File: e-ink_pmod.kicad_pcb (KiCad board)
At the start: 2 copper layers, 45.7 x 20.3 mm, 1 part

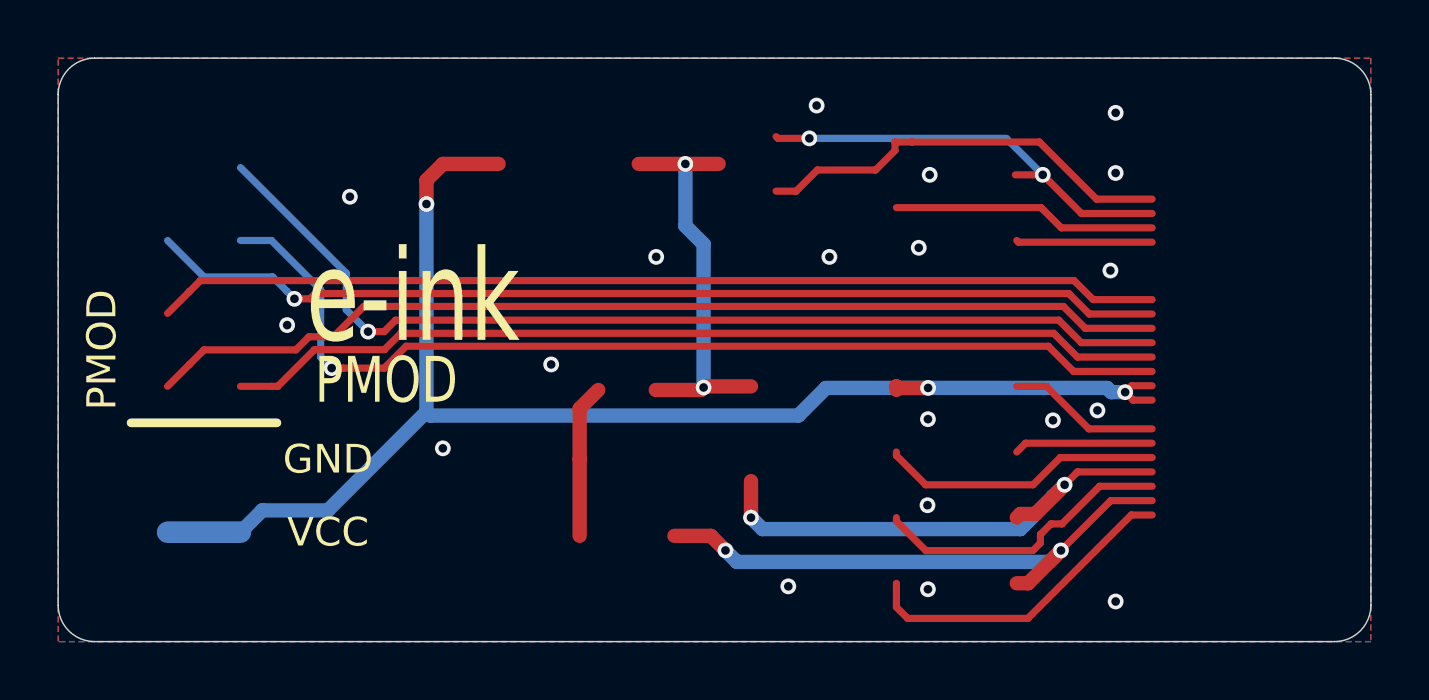
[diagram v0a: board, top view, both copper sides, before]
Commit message: Added SPI SRAM for framebuffer
Also updated to new KiCad version 6 file formats
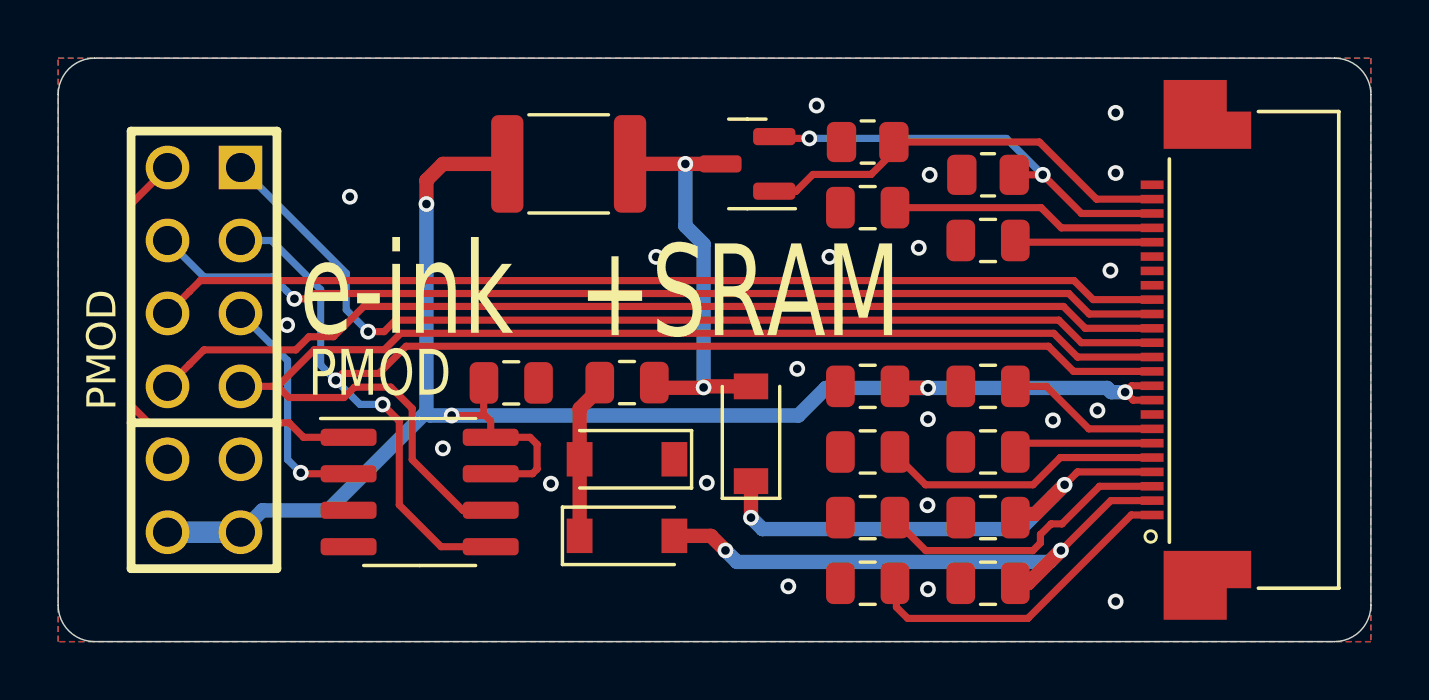
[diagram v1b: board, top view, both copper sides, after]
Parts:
- added C1: 1uF, Capacitor_SMD:C_0805_2012Metric, F.Cu at (114.6, 75.1)
- added C10: 2.2uF, Capacitor_SMD:C_0805_2012Metric, F.Cu at (114.6, 81.3)
- added C11: 1uF, Capacitor_SMD:C_0805_2012Metric, F.Cu at (118.7, 83.6)
- added C12: 1uF, Capacitor_SMD:C_0805_2012Metric, F.Cu at (102.1, 81.2)
- added C2: 1uF, Capacitor_SMD:C_0805_2012Metric, F.Cu at (118.7, 76.2)
- added C3: 1uF, Capacitor_SMD:C_0805_2012Metric, F.Cu at (118.7, 81.3)
- added C4: 1uF, Capacitor_SMD:C_0805_2012Metric, F.Cu at (114.6, 83.6)
- added C5: 1uF, Capacitor_SMD:C_0805_2012Metric, F.Cu at (114.6, 85.9)
- added C6: 1uF, Capacitor_SMD:C_0805_2012Metric, F.Cu at (114.6, 88.1)
- added C7: 1uF, Capacitor_SMD:C_0805_2012Metric, F.Cu at (118.7, 85.9)
- added C8: 1uF, Capacitor_SMD:C_0805_2012Metric, F.Cu at (118.7, 88.1)
- added C9: 1uF, Capacitor_SMD:C_0805_2012Metric, F.Cu at (106.2, 81.2)
- added D1: D_Schottky, Diode_SMD:D_SOD-123, F.Cu at (106.2, 86.5)
- added D2: D_Schottky, Diode_SMD:D_SOD-123, F.Cu at (106.2, 83.8)
- added D3: D_Schottky, Diode_SMD:D_SOD-123, F.Cu at (110.5, 82.9)
- added G***: LOGO, Aesthetics:HXR_logo_small, B.Cu at (126.8, 80.0)
- added L1: 68uH, Inductor_SMD:L_1812_4532Metric, F.Cu at (104.1, 73.5)
- added Q1: Q_NMOS_GSD, Package_TO_SOT_SMD:SOT-23, F.Cu at (110.4, 73.5)
- added R1: 10K, Resistor_SMD:R_0805_2012Metric, F.Cu at (114.6, 72.8)
- added R2: 2.2R, Resistor_SMD:R_0805_2012Metric, F.Cu at (118.7, 73.9)
- added U1: 23K640-I/SN, Package_SO:SOIC-8_3.9x4.9mm_P1.27mm, F.Cu at (99.0, 85.0)
- added X1: 52435-2471, Connectors:MOLEX_52435-2471, F.Cu at (124.5, 80.0)
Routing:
- net COPI: track 0.00 -> 45.7 mm, vias 0 -> 2
- net SCLK: track 0.00 -> 43.4 mm
- net EINK_MOSI: track 35.6 -> 0.00 mm, vias 1 -> 0
- net EINK_SCLK: track 32.9 -> 0.00 mm
- net SRAM_CS: track 0.00 -> 16.8 mm
- net CIPO: track 0.00 -> 8.10 mm, vias 0 -> 1
- net +3V3: track 49.8 -> 57.0 mm, vias 3 -> 4
- net GND: vias 19 -> 21
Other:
- net class Default removed
- board text added: "+SRAM"
- board text added: "CIPO"
- board text added: "COPI"
- board text added: "rev. 1.1"
- board text added: "~BUSY"
- board text added: "~D/C"
- board text added: "~EINKCS"
- board text added: "~RESET"
- board text added: "~SRAMCS"
- board text removed: "BUSY#"
- board text removed: "CS#"
- board text removed: "D/C#"
- board text removed: "MOSI"
- board text removed: "NC"
- board text removed: "RESET#"
